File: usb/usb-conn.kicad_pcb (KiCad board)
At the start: 2 copper layers, 25 x 12 mm, 8 parts, among them J1 Conn_01x04_Pin, J2 Conn_01x04_Pin, J3 USB_C_Receptacle_USB2.0_14P, J4 Conn_01x04_Pin, J5 Conn_01x06_Pin, U1 SPX3819M5-L-3-3

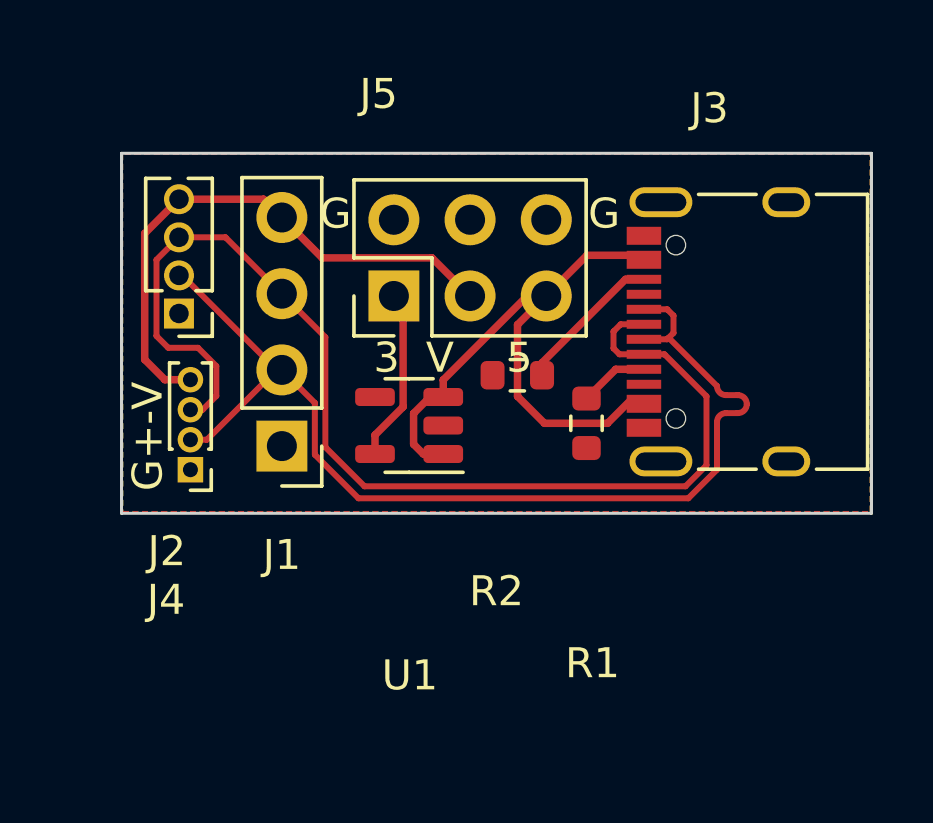
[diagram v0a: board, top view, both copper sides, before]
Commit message: usb: add 2.0 pinout
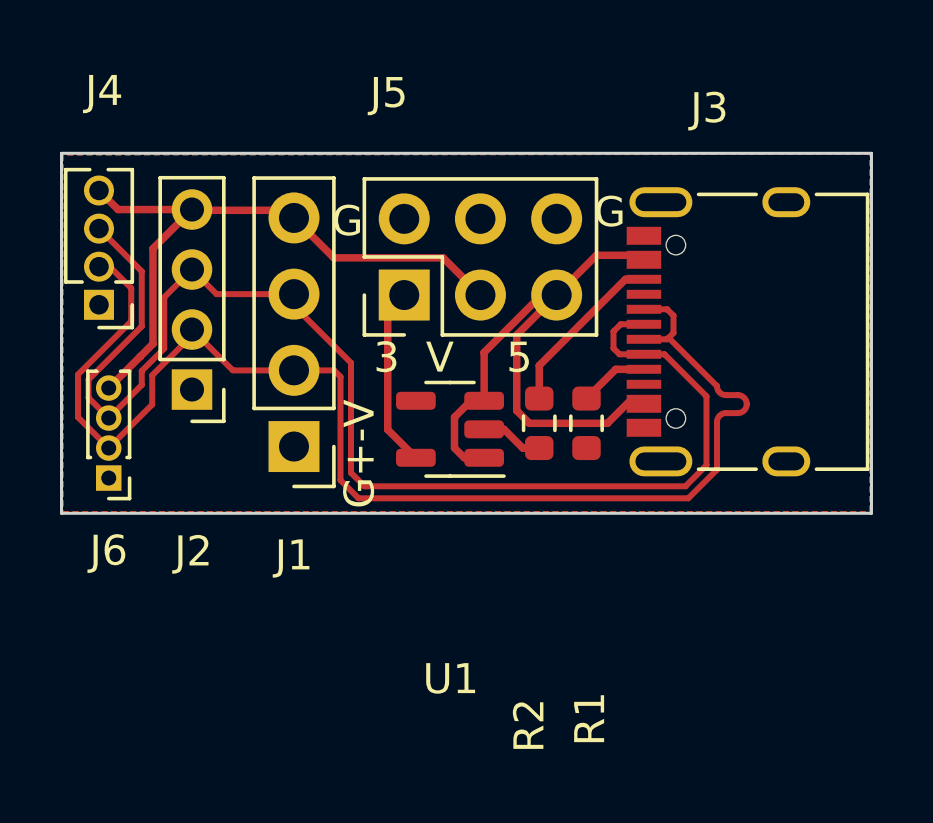
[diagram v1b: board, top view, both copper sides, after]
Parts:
- added J6: Conn_01x04_Pin, Connector_PinHeader_1.00mm:PinHeader_1x04_P1.00mm_Vertical, F.Cu at (114.6, 85.8)
- J2: footprint Connector_PinHeader_1.27mm:PinHeader_1x04_P1.27mm_Vertical -> Connector_PinHeader_2.00mm:PinHeader_1x04_P2.00mm_Vertical
- J4: footprint Connector_PinHeader_1.00mm:PinHeader_1x04_P1.00mm_Vertical -> Connector_PinHeader_1.27mm:PinHeader_1x04_P1.27mm_Vertical
- moved J4 6.29 mm to (114.2, 80.0)
- moved J2 2.57 mm to (117.3, 82.9)
- moved R2 1.76 mm to (128.9, 84.0), turned to 90 degrees
- moved U1 1.37 mm to (126.0, 84.2)
- moved J1 0.41 mm to (120.8, 84.8)
- moved J5 0.35 mm to (124.4, 79.7)
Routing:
- net /D+: track 35.5 -> 44.4 mm
- net /D-: track 39.3 -> 44.6 mm
- net /VOUT: track 18.7 -> 21.3 mm
- net GND: track 0.00 -> 2.10 mm
- net Net-(J3-CC2): track 4.96 -> 5.78 mm
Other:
- board size 25 x 12 mm -> 27 x 12 mm

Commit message: usb-conn: move trace away from board edge
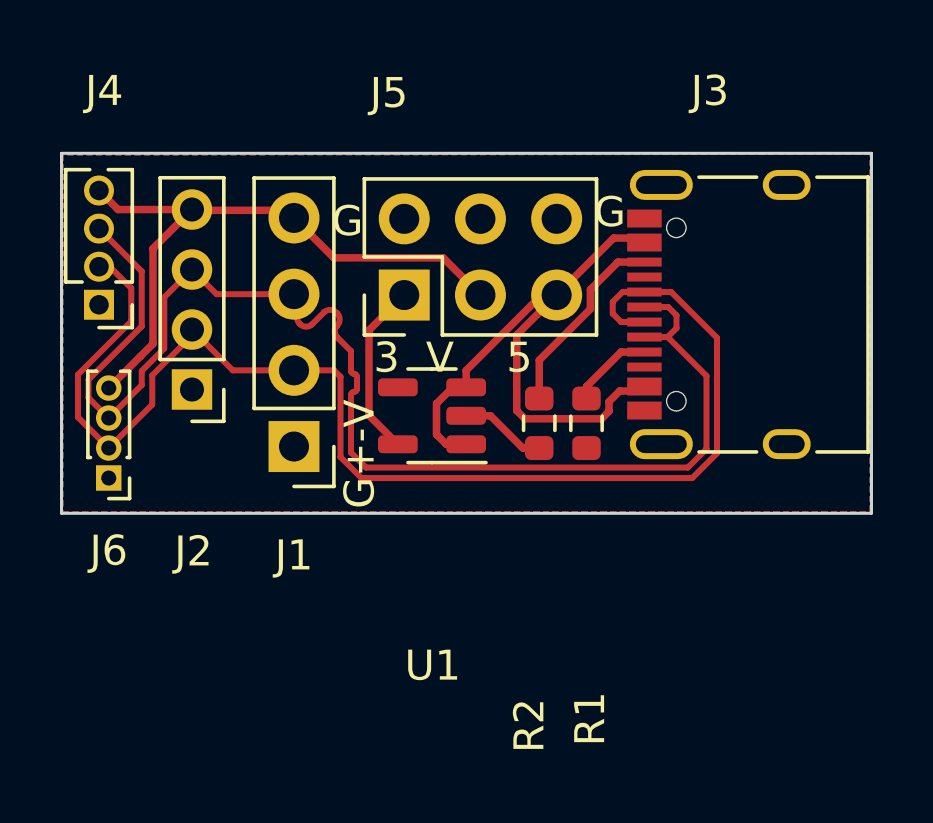
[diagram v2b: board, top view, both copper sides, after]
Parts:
- moved U1 0.75 mm to (125.3, 83.8)
- moved J3 0.58 mm to (136.1, 80.4)
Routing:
- net GND: track 2.10 -> 2.88 mm
- net Net-(J3-CC2): track 5.78 -> 6.52 mm
